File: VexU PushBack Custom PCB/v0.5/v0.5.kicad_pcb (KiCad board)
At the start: 2 copper layers, 40.5 x 70 mm, 40 parts, among them J1 4P4C, J2 Conn_01x04_Pin, U1 Teensy4.1, U2 MP2338GTL-P, U3 4069, U4 MAX485E

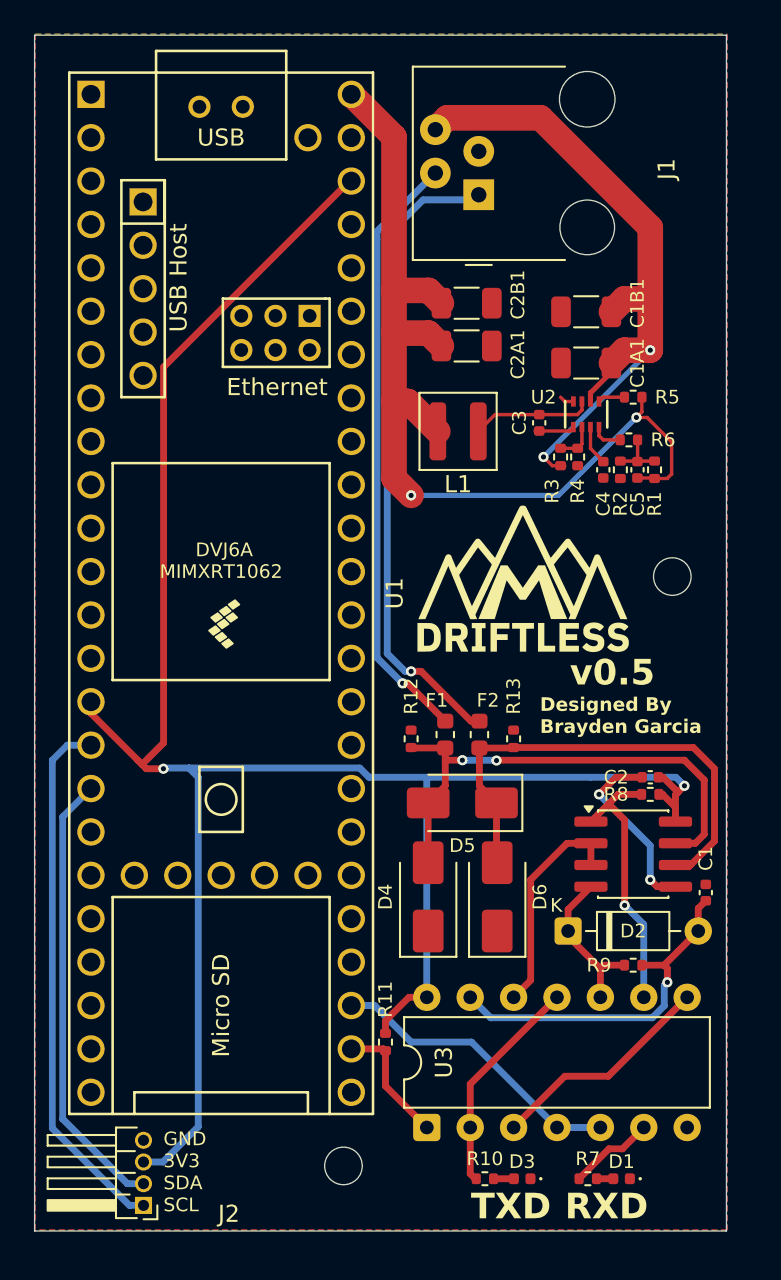
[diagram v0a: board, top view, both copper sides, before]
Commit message: Finishied Schematic
Start work on 4 layer board tracing
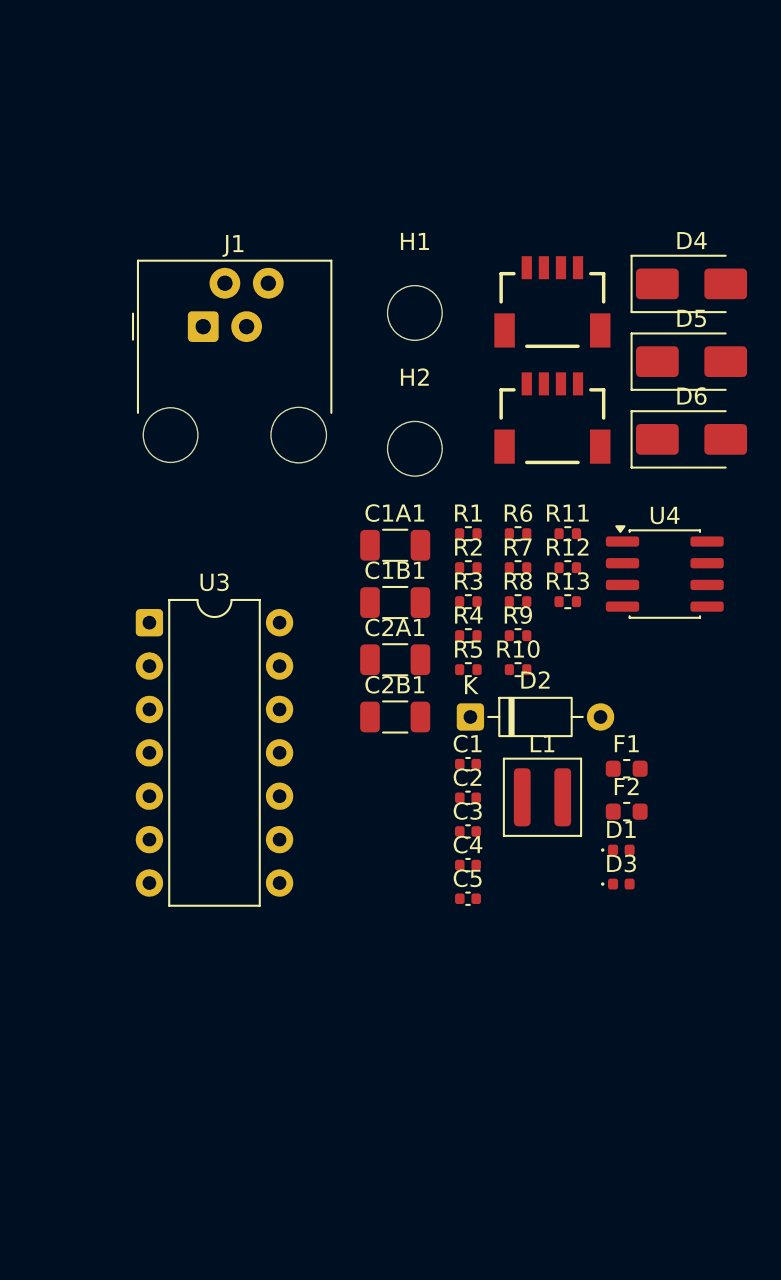
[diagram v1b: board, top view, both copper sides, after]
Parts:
- removed G***: LOGO, LOGO
- removed U1: Teensy4.1, teensy.pretty-master:Teensy41
- removed U2: MP2338GTL-P, MP2338:SOT583_MP2338_MNP
- added J3: Qwiic_RA, SparkFun-Connector:JST_1x04_P1.0mm_Horizontal_SMD, F.Cu at (115.5, 44.2)
- H1, H2: footprint MountingHole:MountingHole_2.2mm_M2 -> MountingHole:MountingHole_3.2mm_M3
- J2: value Conn_01x04_Pin -> Qwiic_RA; footprint Connector_PinHeader_1.27mm:PinHeader_1x04_P1.27mm_Horizontal -> SparkFun-Connector:JST_1x04_P1.0mm_Horizontal_SMD
- moved J2 59.9 mm to (115.5, 37.4), turned to 0 degrees
- moved H2 42.2 mm to (107.4, 48.0), turned to 0 degrees
- moved D4 39.1 mm to (123.6, 38.4), turned to 0 degrees
- moved R7 36.0 mm to (113.5, 55.0)
- moved U3 33.7 mm to (91.9, 58.2), turned to 0 degrees
- moved R11 31.6 mm to (116.4, 53.0), turned to 0 degrees
- moved R10 29.9 mm to (113.5, 61.0)
- moved D5 29.1 mm to (123.6, 42.9), turned to 0 degrees
- moved D6 29.1 mm to (123.6, 47.5), turned to 0 degrees
- moved C5 27.0 mm to (110.5, 74.4), turned to 0 degrees
- moved C2B1 24.6 mm to (106.3, 63.7)
- moved C4 24.5 mm to (110.5, 72.4), turned to 0 degrees
- moved C3 24.3 mm to (110.5, 70.4), turned to 0 degrees
- moved L1 22.0 mm to (114.9, 68.4), turned to 0 degrees
- moved H1 21.6 mm to (107.4, 40.1), turned to 0 degrees
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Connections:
- J2 pad 1: SCL -> GND
- J2 pad 2: SDA -> 3V3
- J2 pad 3: 3V3 -> OTOS_SDA
- J2 pad 4: GND -> OTOS_SCL
- R11 pad 2: RXD -> TXD
- U3 pad 1: RXD -> TXD
- U3 pad 4: TXD -> RXD
- U3 pad 5: TXD -> RXD
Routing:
- net 3V3: track 123.5 -> 0.00 mm, vias 2 -> 0
- net 5V: track 57.4 -> 0.00 mm, vias 2 -> 0
- net 12V: track 40.9 -> 0.00 mm, vias 2 -> 0
- net A: track 37.8 -> 0.00 mm, vias 1 -> 0
- net B: track 35.3 -> 0.00 mm, vias 1 -> 0
- net SCL: track 31.4 -> 0.00 mm
- net Net-(D4-A2): track 30.0 -> 0.00 mm, vias 2 -> 0
- net Net-(D5-A1): track 28.6 -> 0.00 mm
- net SDA: track 26.3 -> 0.00 mm
- net Net-(D2-A): track 20.8 -> 0.00 mm, vias 1 -> 0
- net TXD: track 17.5 -> 0.00 mm
- net Net-(U4-RO): track 15.8 -> 0.00 mm, vias 1 -> 0
- net Net-(U3-Pad3): track 13.3 -> 0.00 mm
- net Net-(U4-DE): track 13.0 -> 0.00 mm
- net Net-(R10-Pad1): track 12.9 -> 0.00 mm
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- removed copper zone on B.Cu, net GND
- removed copper zone on F.Cu, net GND
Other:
- board outline removed
- board text removed: "Designed By Brayden Garcia"
- board text removed: "GND 3V3 SDA SCL"
- board text removed: "RXD"
- board text removed: "TXD"
- board text removed: "v0.5"

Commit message: Finished Routing PCB
Pushed For production
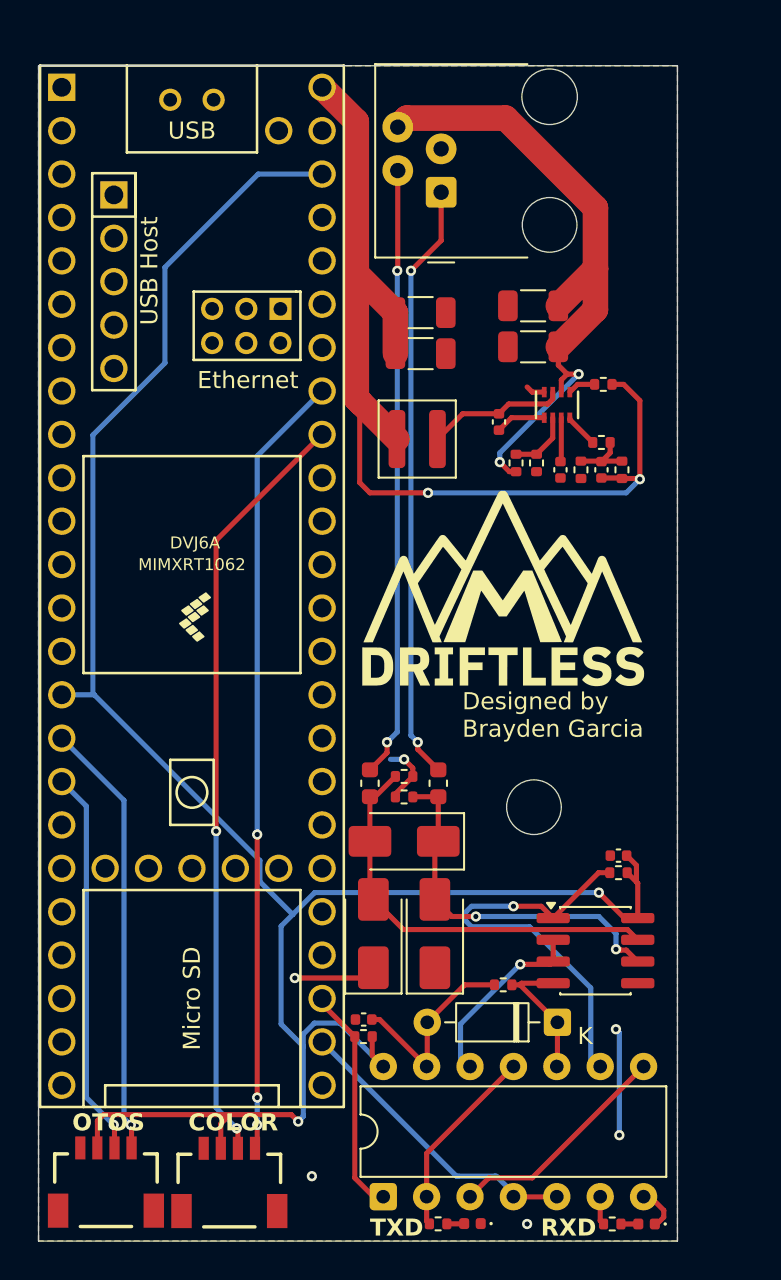
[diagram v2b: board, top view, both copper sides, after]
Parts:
- removed H1: MountingHole, MountingHole:MountingHole_3.2mm_M3
- added G***: LOGO, LOGO, F.Cu at (112.6, 58.4)
- added U1: Teensy4.1, teensy.pretty-master:Teensy41, F.Cu at (94.4, 56.1)
- added U2: MP2338GTL-P, MP2338:SOT583_MP2338_MNP, F.Cu at (115.8, 45.5)
- moved J2 57.8 mm to (89.3, 88.9)
- moved J3 48.6 mm to (96.6, 89.0)
- moved D4 42.3 mm to (105.0, 76.4), turned to 90 degrees
- moved R7 38.8 mm to (119.0, 93.4)
- moved U3 36.3 mm to (105.6, 91.8), turned to 90 degrees
- moved R10 32.8 mm to (108.8, 93.4)
- moved D5 32.7 mm to (106.8, 71.0), turned to 180 degrees
- moved D6 32.6 mm to (108.6, 76.4), turned to 90 degrees
- moved R11 31.8 mm to (104.4, 82.4), turned to 180 degrees
- moved C5 26.3 mm to (118.4, 49.3), turned to -90 degrees
- moved C3 24.0 mm to (112.4, 46.5), turned to 90 degrees
- moved C4 23.8 mm to (116.0, 49.3), turned to -90 degrees
- moved U4 22.4 mm to (118.0, 77.4)
- moved L1 22.2 mm to (107.6, 47.5), turned to 180 degrees
- moved H2 22.1 mm to (114.4, 69.0)
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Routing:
- net 3V3: track 0.00 -> 121.8 mm, vias 0 -> 2
- net 5V: track 0.00 -> 58.6 mm, vias 0 -> 2
- net COLOR_SCL: track 0.00 -> 46.0 mm, vias 0 -> 3
- net COLOR_SDA: track 0.00 -> 44.9 mm, vias 0 -> 2
- net 12V: track 0.00 -> 38.0 mm, vias 0 -> 2
- net B: track 0.00 -> 35.8 mm, vias 0 -> 2
- net A: track 0.00 -> 35.2 mm, vias 0 -> 2
- net OTOS_SCL: track 0.00 -> 25.7 mm, vias 0 -> 1
- net Net-(D4-A2): track 0.00 -> 24.5 mm
- net Net-(U4-RO): track 0.00 -> 24.0 mm, vias 0 -> 1
- net OTOS_SDA: track 0.00 -> 22.7 mm, vias 0 -> 1
- net Net-(D5-A1): track 0.00 -> 21.5 mm, vias 0 -> 2
- net GND: track 0.00 -> 18.8 mm, vias 0 -> 6
- net RXD: track 0.00 -> 17.7 mm
- net Net-(U3-Pad3): track 0.00 -> 13.3 mm
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- added copper zone on B.Cu, net GND
- added copper zone on F.Cu, net GND
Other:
- board outline added: 37.4 x 68.8 mm
- board text added: "COLOR"
- board text added: "Designed by Brayden Garcia"
- board text added: "OTOS"
- board text added: "RXD"
- board text added: "TXD"

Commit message: Worlds Push
Season Over
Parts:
- added G***: LOGO, LOGO, B.Cu at (114.0, 56.7)
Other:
- board text added: "I AM SMILING FROM EAR TO EAR"
